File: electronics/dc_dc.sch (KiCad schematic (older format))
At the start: 14 parts

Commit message: Slightly change electronics
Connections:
- net labels added: VCC
- net labels removed: 5V
- wire segments 47 -> 41
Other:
- moved on the sheet: C?, D?, L?, R?
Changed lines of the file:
@@
 L Device:C C?
 U 1 1 5E8CFB92
-P 4500 3600
-F 0 "C?" H 4615 3646 50  0000 L CNN
-F 1 "C" H 4615 3555 50  0000 L CNN
-F 2 "" H 4538 3450 50  0001 C CNN
-F 3 "~" H 4500 3600 50  0001 C CNN
-	1    4500 3600
+P 4850 3000
+F 0 "C?" H 4965 3046 50  0000 L CNN
+F 1 "C" H 4965 2955 50  0000 L CNN
+F 2 "" H 4888 2850 50  0001 C CNN
+F 3 "~" H 4850 3000 50  0001 C CNN
+	1    4850 3000
 	1    0    0    -1
 $EndComp
@@
 L Device:C C?
 U 1 1 5E8D269D
-P 7250 3350
-F 0 "C?" H 7365 3396 50  0000 L CNN
-F 1 "C" H 7365 3305 50  0000 L CNN
-F 2 "" H 7288 3200 50  0001 C CNN
-F 3 "~" H 7250 3350 50  0001 C CNN
-	1    7250 3350
-	1    0    0    -1
+P 7250 3000
+F 0 "C?" H 7365 3046 50  0000 L CNN
+F 1 "C" H 7365 2955 50  0000 L CNN
+F 2 "" H 7288 2850 50  0001 C CNN
+F 3 "~" H 7250 3000 50  0001 C CNN
+	1    7250 3000
+	-1   0    0    1
 $EndComp
 $Comp
@@
 L Device:R R?
 U 1 1 5E8D49A8
-P 7600 3400
-F 0 "R?" H 7670 3446 50  0000 L CNN
-F 1 "R" H 7670 3355 50  0000 L CNN
-F 2 "" V 7530 3400 50  0001 C CNN
-F 3 "~" H 7600 3400 50  0001 C CNN
-	1    7600 3400
+P 7250 3550
+F 0 "R?" H 7320 3596 50  0000 L CNN
+F 1 "R" H 7320 3505 50  0000 L CNN
+F 2 "" V 7180 3550 50  0001 C CNN
+F 3 "~" H 7250 3550 50  0001 C CNN
+	1    7250 3550
 	1    0    0    -1
 $EndComp
@@
 	-1   0    0    1
 $EndComp
-Wire Wire Line
-	4500 3350 4300 3350
-Connection ~ 4500 3350
 $Comp
 L Device:R R?
@@
 	1    0    0    -1
 $EndComp
-$Comp
-L power:GND #PWR0102
-U 1 1 5E8DAC8B
-P 4500 3850
-F 0 "#PWR0102" H 4500 3600 50  0001 C CNN
-F 1 "GND" H 4505 3677 50  0000 C CNN
-F 2 "" H 4500 3850 50  0001 C CNN
-F 3 "" H 4500 3850 50  0001 C CNN
-	1    4500 3850
-	1    0    0    -1
-$EndComp
 Wire Wire Line
 	4850 4150 4850 3900
 Connection ~ 4850 3900
-Wire Wire Line
-	4850 3900 4700 3900
 Wire Wire Line
 	5700 3450 5700 3350
@@
 L Device:L L?
 U 1 1 5E8EE125
-P 6950 3100
-F 0 "L?" V 7140 3100 50  0000 C CNN
-F 1 "L" V 7049 3100 50  0000 C CNN
-F 2 "" H 6950 3100 50  0001 C CNN
-F 3 "~" H 6950 3100 50  0001 C CNN
-	1    6950 3100
+P 6750 3350
+F 0 "L?" V 6940 3350 50  0000 C CNN
+F 1 "L" V 6849 3350 50  0000 C CNN
+F 2 "" H 6750 3350 50  0001 C CNN
+F 3 "~" H 6750 3350 50  0001 C CNN
+	1    6750 3350
 	0    -1   -1   0
 $EndComp
@@
 L Device:D_Schottky D?
 U 1 1 5E8EE734
-P 6600 3350
-F 0 "D?" V 6554 3429 50  0000 L CNN
-F 1 "D_Schottky" V 6645 3429 50  0000 L CNN
-F 2 "" H 6600 3350 50  0001 C CNN
-F 3 "~" H 6600 3350 50  0001 C CNN
-	1    6600 3350
-	0    1    1    0
+P 6500 3000
+F 0 "D?" V 6454 3079 50  0000 L CNN
+F 1 "D_Schottky" V 6545 3079 50  0000 L CNN
+F 2 "" H 6500 3000 50  0001 C CNN
+F 3 "~" H 6500 3000 50  0001 C CNN
+	1    6500 3000
+	0    -1   -1   0
 $EndComp
 $Comp
 L power:GND #PWR0106
 U 1 1 5E8F0C8B
-P 6600 3550
-F 0 "#PWR0106" H 6600 3300 50  0001 C CNN
-F 1 "GND" H 6605 3377 50  0000 C CNN
-F 2 "" H 6600 3550 50  0001 C CNN
-F 3 "" H 6600 3550 50  0001 C CNN
-	1    6600 3550
-	1    0    0    -1
+P 6500 2750
+F 0 "#PWR0106" H 6500 2500 50  0001 C CNN
+F 1 "GND" H 6505 2577 50  0000 C CNN
+F 2 "" H 6500 2750 50  0001 C CNN
+F 3 "" H 6500 2750 50  0001 C CNN
+	1    6500 2750
+	-1   0    0    1
 $EndComp
 $Comp
 L power:GND #PWR0107
 U 1 1 5E8F68C8
-P 7250 3550
-F 0 "#PWR0107" H 7250 3300 50  0001 C CNN
-F 1 "GND" H 7255 3377 50  0000 C CNN
-F 2 "" H 7250 3550 50  0001 C CNN
-F 3 "" H 7250 3550 50  0001 C CNN
-	1    7250 3550
-	1    0    0    -1
-$EndComp
-Wire Wire Line
-	6600 3550 6600 3500
-Wire Wire Line
-	7250 3550 7250 3500
-Wire Wire Line
-	6300 3350 6300 3100
-Wire Wire Line
-	6300 3100 6600 3100
+P 7250 2750
+F 0 "#PWR0107" H 7250 2500 50  0001 C CNN
+F 1 "GND" H 7255 2577 50  0000 C CNN
+F 2 "" H 7250 2750 50  0001 C CNN
+F 3 "" H 7250 2750 50  0001 C CNN
+	1    7250 2750
+	-1   0    0    1
+$EndComp
+Wire Wire Line
+	6500 2750 6500 2850
+Wire Wire Line
+	7250 2750 7250 2850
 Connection ~ 6300 3350
 Wire Wire Line
-	6600 3200 6600 3100
-Connection ~ 6600 3100
-Wire Wire Line
-	6600 3100 6800 3100
-Wire Wire Line
-	7100 3100 7250 3100
-Wire Wire Line
-	7250 3100 7250 3200
-Wire Wire Line
 	6200 3800 7250 3800
 Wire Wire Line
 	7250 3800 7250 4000
 Wire Wire Line
-	7250 3800 7600 3800
-Wire Wire Line
-	7600 3800 7600 3550
-Connection ~ 7250 3800
-Wire Wire Line
-	7600 3250 7600 3100
-Wire Wire Line
-	7600 3100 7250 3100
-Connection ~ 7250 3100
+	7250 3800 7250 3700
 Wire Wire Line
 	7250 4300 7250 4700
@@
 $EndComp
 Wire Wire Line
-	4500 3350 4850 3350
-Wire Wire Line
 	4850 3350 4850 3450
 Connection ~ 4850 3350
 Wire Wire Line
-	4500 3350 4500 3450
-Wire Wire Line
 	4850 3750 4850 3900
-Wire Wire Line
-	7600 3100 7800 3100
-Connection ~ 7600 3100
-Wire Wire Line
-	4500 3850 4500 3750
-Text Label 7700 3100 0    50   ~ 0
-5V
-Text Label 4300 3350 0    50   ~ 0
+Text Label 8150 3350 0    50   ~ 0
+VCC
+Text Label 3250 3350 0    50   ~ 0
 BATT
-Wire Wire Line
-	4300 4300 4700 4300
-Wire Wire Line
-	4700 3900 4700 4300
-Text Label 4300 4300 0    50   ~ 0
+Text Label 3250 3900 0    50   ~ 0
 EN
 Wire Wire Line
@@
 Wire Wire Line
 	4850 4500 4850 4700
+Wire Wire Line
+	3250 3350 4850 3350
+Wire Wire Line
+	3250 3900 4850 3900
+Wire Wire Line
+	4850 3150 4850 3350
+Wire Wire Line
+	4850 2850 4850 2750
+$Comp
+L power:GND #PWR?
+U 1 1 5E932930
+P 4850 2750
+F 0 "#PWR?" H 4850 2500 50  0001 C CNN
+F 1 "GND" H 4855 2577 50  0000 C CNN
+F 2 "" H 4850 2750 50  0001 C CNN
+F 3 "" H 4850 2750 50  0001 C CNN
+	1    4850 2750
+	-1   0    0    1
+$EndComp
+Wire Wire Line
+	6300 3350 6500 3350
+Connection ~ 7250 3800
+Wire Wire Line
+	6900 3350 7250 3350
+Connection ~ 7250 3350
+Wire Wire Line
+	7250 3350 7250 3400
+Wire Wire Line
+	7250 3350 8250 3350
+Wire Wire Line
+	6500 3150 6500 3350
+Connection ~ 6500 3350
+Wire Wire Line
+	6500 3350 6600 3350
+Wire Wire Line
+	7250 3150 7250 3350
 $EndSCHEMATC

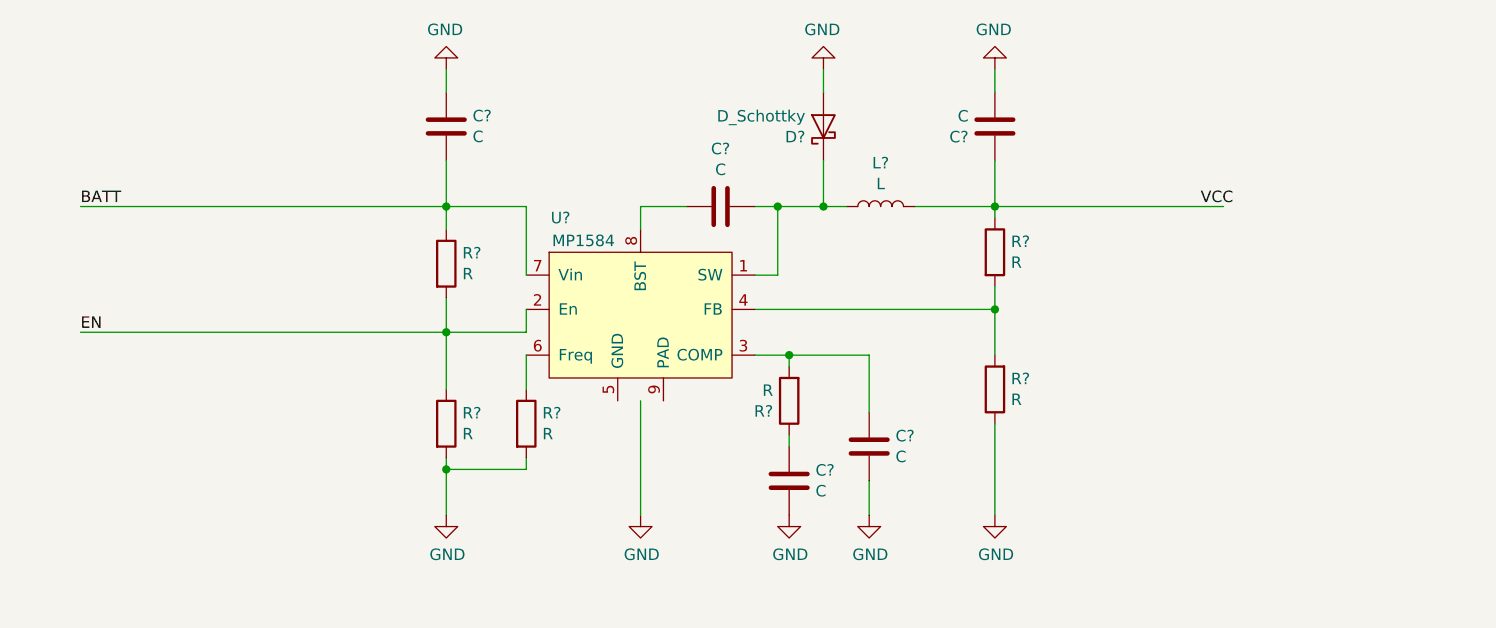
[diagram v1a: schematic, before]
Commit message: Update DCDC design, add a DCDC output calculator tool, add oled screen 3D models
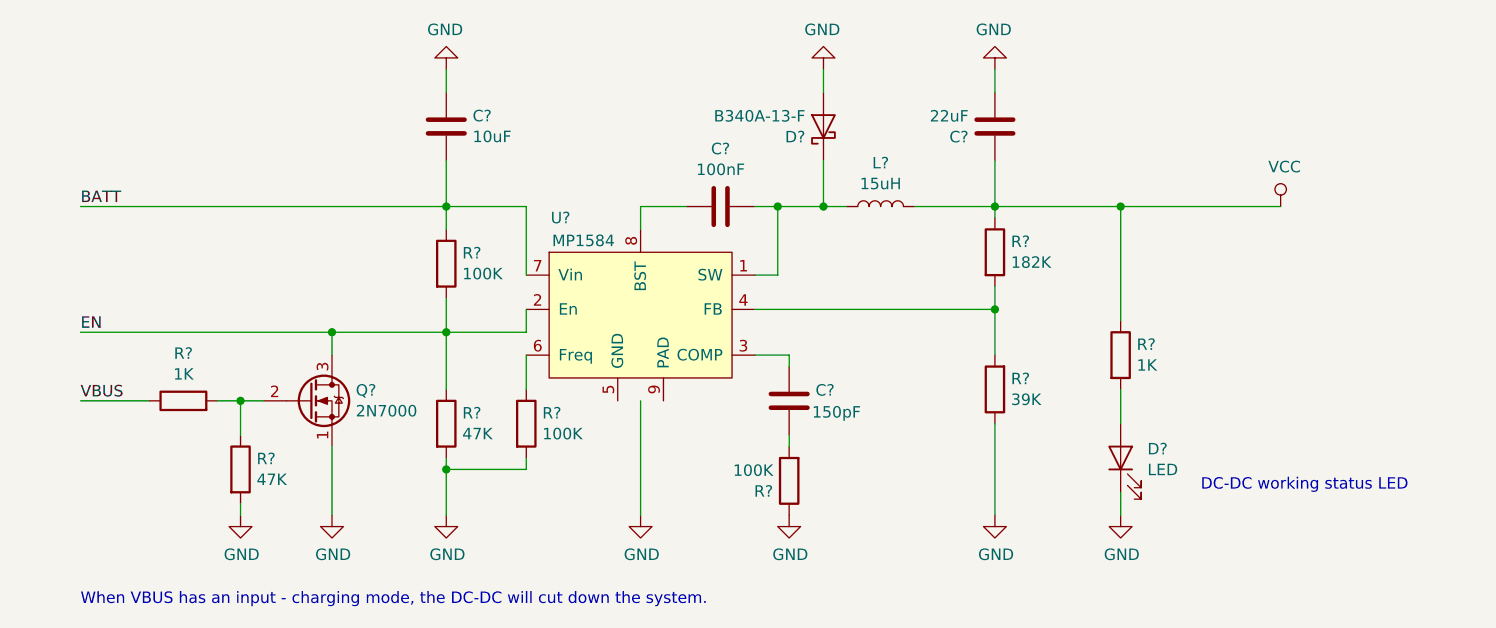
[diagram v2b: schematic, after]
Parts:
- removed C?: C, symbol Device:C
- added D?: LED, LED_SMD:LED_0805_2012Metric, symbol Device:LED
- added Q?: 2N7000, Package_TO_SOT_SMD:SOT-23, symbol Transistor_FET:2N7000
- added R? (x2): 1K, Resistor_SMD:R_0805_2012Metric, symbol Device:R
- added R?: 47K, Resistor_SMD:R_0805_2012Metric, symbol Device:R
- C?: value C -> 10uF; footprint (none) -> Capacitor_SMD:C_1206_3216Metric
- C?: value C -> 100nF; footprint (none) -> Capacitor_SMD:C_0805_2012Metric
- C?: value C -> 22uF; footprint (none) -> Capacitor_SMD:C_1206_3216Metric
- C?: value C -> 150pF; footprint (none) -> Capacitor_SMD:C_0805_2012Metric
- D?: value D_Schottky -> B340A-13-F; footprint (none) -> Diode_SMD:D_SMA
- L?: value L -> 15uH; footprint (none) -> Inductor_SMD:L_12x12mm_H6mm
- R? (x3): value R -> 100K; footprint (none) -> Resistor_SMD:R_0805_2012Metric
- R?: value R -> 47K; footprint (none) -> Resistor_SMD:R_0805_2012Metric
- R?: value R -> 182K; footprint (none) -> Resistor_SMD:R_0805_2012Metric
- R?: value R -> 39K; footprint (none) -> Resistor_SMD:R_0805_2012Metric
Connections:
- net labels added: VBUS
- wire segments 41 -> 50
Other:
- note added: "DC-DC working status LED"
- note added: "When VBUS has an input - charging mode, the DC-DC will cut down the system."
- moved on the sheet: C?, R?
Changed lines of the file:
@@
 P 4850 3000
 F 0 "C?" H 4965 3046 50  0000 L CNN
-F 1 "C" H 4965 2955 50  0000 L CNN
-F 2 "" H 4888 2850 50  0001 C CNN
+F 1 "10uF" H 4965 2955 50  0000 L CNN
+F 2 "Capacitor_SMD:C_1206_3216Metric" H 4888 2850 50  0001 C CNN
 F 3 "~" H 4850 3000 50  0001 C CNN
 	1    4850 3000
@@
 P 6050 3350
 F 0 "C?" V 5798 3350 50  0000 C CNN
-F 1 "C" V 5889 3350 50  0000 C CNN
-F 2 "" H 6088 3200 50  0001 C CNN
+F 1 "100nF" V 5889 3350 50  0000 C CNN
+F 2 "Capacitor_SMD:C_0805_2012Metric" H 6088 3200 50  0001 C CNN
 F 3 "~" H 6050 3350 50  0001 C CNN
 	1    6050 3350
@@
 P 4850 3600
 F 0 "R?" H 4920 3646 50  0000 L CNN
-F 1 "R" H 4920 3555 50  0000 L CNN
-F 2 "" V 4780 3600 50  0001 C CNN
+F 1 "100K" H 4920 3555 50  0000 L CNN
+F 2 "Resistor_SMD:R_0805_2012Metric" V 4780 3600 50  0001 C CNN
 F 3 "~" H 4850 3600 50  0001 C CNN
 	1    4850 3600
@@
 P 4850 4300
 F 0 "R?" H 4920 4346 50  0000 L CNN
-F 1 "R" H 4920 4255 50  0000 L CNN
-F 2 "" V 4780 4300 50  0001 C CNN
+F 1 "47K" H 4920 4255 50  0000 L CNN
+F 2 "Resistor_SMD:R_0805_2012Metric" V 4780 4300 50  0001 C CNN
 F 3 "~" H 4850 4300 50  0001 C CNN
 	1    4850 4300
@@
 P 7250 3000
 F 0 "C?" H 7365 3046 50  0000 L CNN
-F 1 "C" H 7365 2955 50  0000 L CNN
-F 2 "" H 7288 2850 50  0001 C CNN
+F 1 "22uF" H 7365 2955 50  0000 L CNN
+F 2 "Capacitor_SMD:C_1206_3216Metric" H 7288 2850 50  0001 C CNN
 F 3 "~" H 7250 3000 50  0001 C CNN
 	1    7250 3000
@@
 L Device:C C?
 U 1 1 5E8D2B29
-P 6350 4550
-F 0 "C?" H 6465 4596 50  0000 L CNN
-F 1 "C" H 6465 4505 50  0000 L CNN
-F 2 "" H 6388 4400 50  0001 C CNN
-F 3 "~" H 6350 4550 50  0001 C CNN
-	1    6350 4550
-	1    0    0    -1
-$EndComp
-$Comp
-L Device:C C?
-U 1 1 5E8D32A5
-P 6700 4400
-F 0 "C?" H 6815 4446 50  0000 L CNN
-F 1 "C" H 6815 4355 50  0000 L CNN
-F 2 "" H 6738 4250 50  0001 C CNN
-F 3 "~" H 6700 4400 50  0001 C CNN
-	1    6700 4400
+P 6350 4200
+F 0 "C?" H 6465 4246 50  0000 L CNN
+F 1 "150pF" H 6450 4150 50  0000 L CNN
+F 2 "Capacitor_SMD:C_0805_2012Metric" H 6388 4050 50  0001 C CNN
+F 3 "~" H 6350 4200 50  0001 C CNN
+	1    6350 4200
 	1    0    0    -1
 $EndComp
@@
 P 7250 3550
 F 0 "R?" H 7320 3596 50  0000 L CNN
-F 1 "R" H 7320 3505 50  0000 L CNN
-F 2 "" V 7180 3550 50  0001 C CNN
+F 1 "182K" H 7320 3505 50  0000 L CNN
+F 2 "Resistor_SMD:R_0805_2012Metric" V 7180 3550 50  0001 C CNN
 F 3 "~" H 7250 3550 50  0001 C CNN
 	1    7250 3550
@@
 L Device:R R?
 U 1 1 5E8D4DEA
-P 6350 4200
-F 0 "R?" H 6420 4246 50  0000 L CNN
-F 1 "R" H 6420 4155 50  0000 L CNN
-F 2 "" V 6280 4200 50  0001 C CNN
-F 3 "~" H 6350 4200 50  0001 C CNN
-	1    6350 4200
+P 6350 4550
+F 0 "R?" H 6420 4596 50  0000 L CNN
+F 1 "100K" H 6420 4505 50  0000 L CNN
+F 2 "Resistor_SMD:R_0805_2012Metric" V 6280 4550 50  0001 C CNN
+F 3 "~" H 6350 4550 50  0001 C CNN
+	1    6350 4550
 	-1   0    0    1
 $EndComp
@@
 P 5200 4300
 F 0 "R?" H 5270 4346 50  0000 L CNN
-F 1 "R" H 5270 4255 50  0000 L CNN
-F 2 "" V 5130 4300 50  0001 C CNN
+F 1 "100K" H 5270 4255 50  0000 L CNN
+F 2 "Resistor_SMD:R_0805_2012Metric" V 5130 4300 50  0001 C CNN
 F 3 "~" H 5200 4300 50  0001 C CNN
 	1    5200 4300
@@
 Wire Wire Line
 	5700 4200 5700 4700
-Wire Wire Line
-	6700 4000 6350 4000
-Connection ~ 6350 4000
-Wire Wire Line
-	6700 4000 6700 4250
-Wire Wire Line
-	6700 4550 6700 4700
-$Comp
-L power:GND #PWR0105
-U 1 1 5E8EBD06
-P 6700 4700
-F 0 "#PWR0105" H 6700 4450 50  0001 C CNN
-F 1 "GND" H 6705 4527 50  0000 C CNN
-F 2 "" H 6700 4700 50  0001 C CNN
-F 3 "" H 6700 4700 50  0001 C CNN
-	1    6700 4700
-	1    0    0    -1
-$EndComp
 $Comp
 L Device:R R?
@@
 P 7250 4150
 F 0 "R?" H 7180 4104 50  0000 R CNN
-F 1 "R" H 7180 4195 50  0000 R CNN
-F 2 "" V 7180 4150 50  0001 C CNN
+F 1 "39K" H 7180 4195 50  0000 R CNN
+F 2 "Resistor_SMD:R_0805_2012Metric" V 7180 4150 50  0001 C CNN
 F 3 "~" H 7250 4150 50  0001 C CNN
 	1    7250 4150
@@
 P 6750 3350
 F 0 "L?" V 6940 3350 50  0000 C CNN
-F 1 "L" V 6849 3350 50  0000 C CNN
-F 2 "" H 6750 3350 50  0001 C CNN
+F 1 "15uH" V 6849 3350 50  0000 C CNN
+F 2 "Inductor_SMD:L_12x12mm_H6mm" H 6750 3350 50  0001 C CNN
 F 3 "~" H 6750 3350 50  0001 C CNN
 	1    6750 3350
@@
 P 6500 3000
 F 0 "D?" V 6454 3079 50  0000 L CNN
-F 1 "D_Schottky" V 6545 3079 50  0000 L CNN
-F 2 "" H 6500 3000 50  0001 C CNN
+F 1 "B340A-13-F" V 6545 3079 50  0000 L CNN
+F 2 "Diode_SMD:D_SMA" H 6500 3000 50  0001 C CNN
 F 3 "~" H 6500 3000 50  0001 C CNN
 	1    6500 3000
@@
 Wire Wire Line
 	4850 3750 4850 3900
-Text Label 8150 3350 0    50   ~ 0
-VCC
 Text Label 3250 3350 0    50   ~ 0
 BATT
@@
 Wire Wire Line
 	3250 3350 4850 3350
-Wire Wire Line
-	3250 3900 4850 3900
 Wire Wire Line
 	4850 3150 4850 3350
@@
 	7250 3350 7250 3400
 Wire Wire Line
-	7250 3350 8250 3350
+	7250 3350 7800 3350
 Wire Wire Line
 	6500 3150 6500 3350
@@
 Wire Wire Line
 	7250 3150 7250 3350
+$Comp
+L power:VCC #PWR?
+U 1 1 5E935E86
+P 8500 3350
+F 0 "#PWR?" H 8500 3200 50  0001 C CNN
+F 1 "VCC" H 8517 3523 50  0000 C CNN
+F 2 "" H 8500 3350 50  0001 C CNN
+F 3 "" H 8500 3350 50  0001 C CNN
+	1    8500 3350
+	1    0    0    -1
+$EndComp
+$Comp
+L Device:R R?
+U 1 1 5E938B26
+P 7800 4000
+F 0 "R?" H 7870 4046 50  0000 L CNN
+F 1 "1K" H 7870 3955 50  0000 L CNN
+F 2 "Resistor_SMD:R_0805_2012Metric" V 7730 4000 50  0001 C CNN
+F 3 "~" H 7800 4000 50  0001 C CNN
+	1    7800 4000
+	1    0    0    -1
+$EndComp
+$Comp
+L Device:LED D?
+U 1 1 5E939213
+P 7800 4450
+F 0 "D?" V 7839 4333 50  0000 R CNN
+F 1 "LED" V 7748 4333 50  0000 R CNN
+F 2 "LED_SMD:LED_0805_2012Metric" H 7800 4450 50  0001 C CNN
+F 3 "~" H 7800 4450 50  0001 C CNN
+	1    7800 4450
+	0    -1   -1   0
+$EndComp
+Wire Wire Line
+	7800 4150 7800 4300
+Wire Wire Line
+	7800 4600 7800 4700
+$Comp
+L power:GND #PWR?
+U 1 1 5E93DD7B
+P 7800 4700
+F 0 "#PWR?" H 7800 4450 50  0001 C CNN
+F 1 "GND" H 7805 4527 50  0000 C CNN
+F 2 "" H 7800 4700 50  0001 C CNN
+F 3 "" H 7800 4700 50  0001 C CNN
+	1    7800 4700
+	1    0    0    -1
+$EndComp
+Wire Wire Line
+	7800 3850 7800 3350
+Connection ~ 7800 3350
+Wire Wire Line
+	7800 3350 8500 3350
+$Comp
+L Transistor_FET:2N7000 Q?
+U 1 1 5E941285
+P 4250 4200
+F 0 "Q?" H 4454 4246 50  0000 L CNN
+F 1 "2N7000" H 4454 4155 50  0000 L CNN
+F 2 "Package_TO_SOT_SMD:SOT-23" H 4450 4125 50  0001 L CIN
+F 3 "https://www.fairchildsemi.com/datasheets/2N/2N7000.pdf" H 4250 4200 50  0001 L CNN
+	1    4250 4200
+	1    0    0    -1
+$EndComp
+$Comp
+L power:GND #PWR?
+U 1 1 5E94311E
+P 4350 4700
+F 0 "#PWR?" H 4350 4450 50  0001 C CNN
+F 1 "GND" H 4355 4527 50  0000 C CNN
+F 2 "" H 4350 4700 50  0001 C CNN
+F 3 "" H 4350 4700 50  0001 C CNN
+	1    4350 4700
+	1    0    0    -1
+$EndComp
+Wire Wire Line
+	4350 4400 4350 4700
+Wire Wire Line
+	4350 3900 4350 4000
+$Comp
+L Device:R R?
+U 1 1 5E9453A6
+P 3700 4200
+F 0 "R?" V 3907 4200 50  0000 C CNN
+F 1 "1K" V 3816 4200 50  0000 C CNN
+F 2 "Resistor_SMD:R_0805_2012Metric" V 3630 4200 50  0001 C CNN
+F 3 "~" H 3700 4200 50  0001 C CNN
+	1    3700 4200
+	0    -1   -1   0
+$EndComp
+$Comp
+L Device:R R?
+U 1 1 5E94608A
+P 3950 4500
+F 0 "R?" H 4020 4546 50  0000 L CNN
+F 1 "47K" H 4020 4455 50  0000 L CNN
+F 2 "Resistor_SMD:R_0805_2012Metric" V 3880 4500 50  0001 C CNN
+F 3 "~" H 3950 4500 50  0001 C CNN
+	1    3950 4500
+	1    0    0    -1
+$EndComp
+Connection ~ 4350 3900
+Wire Wire Line
+	4350 3900 4850 3900
+Wire Wire Line
+	3250 3900 4350 3900
+$Comp
+L power:GND #PWR?
+U 1 1 5E94BF0D
+P 3950 4700
+F 0 "#PWR?" H 3950 4450 50  0001 C CNN
+F 1 "GND" H 3955 4527 50  0000 C CNN
+F 2 "" H 3950 4700 50  0001 C CNN
+F 3 "" H 3950 4700 50  0001 C CNN
+	1    3950 4700
+	1    0    0    -1
+$EndComp
+Wire Wire Line
+	3850 4200 3950 4200
+Wire Wire Line
+	3950 4350 3950 4200
+Connection ~ 3950 4200
+Wire Wire Line
+	3950 4200 4050 4200
+Wire Wire Line
+	3950 4650 3950 4700
+Wire Wire Line
+	3550 4200 3250 4200
+Text Label 3250 4200 0    50   ~ 0
+VBUS
+Text Notes 3250 5100 0    50   ~ 0
+When VBUS has an input - charging mode, the DC-DC will cut down the system.
+Text Notes 8150 4600 0    50   ~ 0
+DC-DC working status LED
 $EndSCHEMATC

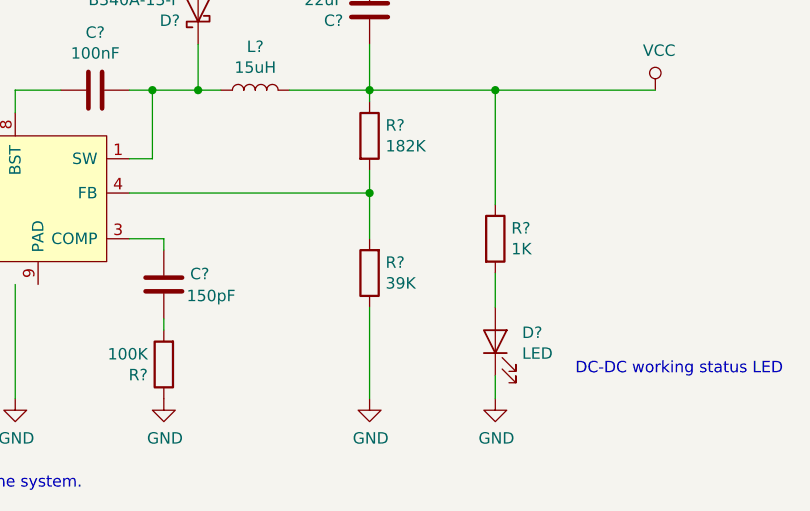
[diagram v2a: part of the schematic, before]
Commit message: Change to electronics, and adding pi dimensions into documents
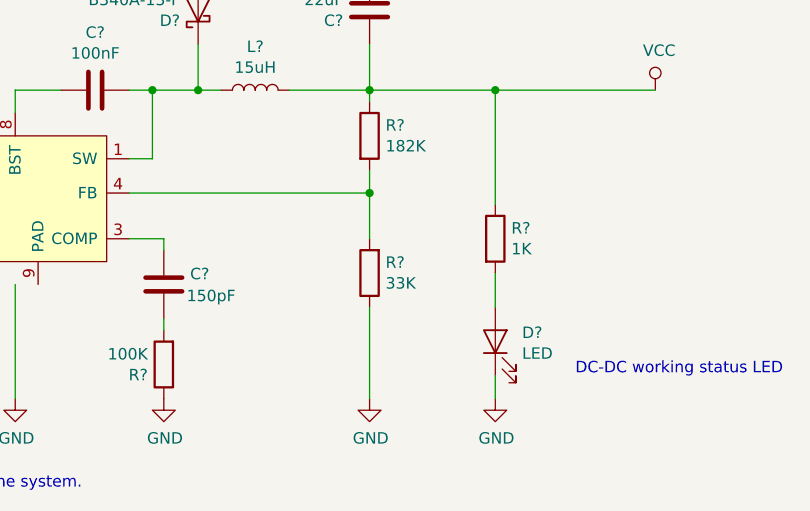
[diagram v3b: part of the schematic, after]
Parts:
- R?: value 39K -> 33K
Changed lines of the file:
@@
 $Descr A4 11693 8268
 encoding utf-8
-Sheet 2 5
+Sheet 2 4
 Title ""
 Date ""
@@
 $EndComp
 $Comp
-L power:GND #PWR0101
+L power:GND #PWR?
 U 1 1 5E8D8C44
 P 4850 4700
-F 0 "#PWR0101" H 4850 4450 50  0001 C CNN
+F 0 "#PWR?" H 4850 4450 50  0001 C CNN
 F 1 "GND" H 4855 4527 50  0000 C CNN
 F 2 "" H 4850 4700 50  0001 C CNN
@@
 	6300 3350 6200 3350
 $Comp
-L power:GND #PWR0103
+L power:GND #PWR?
 U 1 1 5E8E265E
 P 5700 4700
-F 0 "#PWR0103" H 5700 4450 50  0001 C CNN
+F 0 "#PWR?" H 5700 4450 50  0001 C CNN
 F 1 "GND" H 5705 4527 50  0000 C CNN
 F 2 "" H 5700 4700 50  0001 C CNN
@@
 	6350 4350 6350 4400
 $Comp
-L power:GND #PWR0104
+L power:GND #PWR?
 U 1 1 5E8E80EC
 P 6350 4700
-F 0 "#PWR0104" H 6350 4450 50  0001 C CNN
+F 0 "#PWR?" H 6350 4450 50  0001 C CNN
 F 1 "GND" H 6355 4527 50  0000 C CNN
 F 2 "" H 6350 4700 50  0001 C CNN
@@
 P 7250 4150
 F 0 "R?" H 7180 4104 50  0000 R CNN
-F 1 "39K" H 7180 4195 50  0000 R CNN
+F 1 "33K" H 7180 4195 50  0000 R CNN
 F 2 "Resistor_SMD:R_0805_2012Metric" V 7180 4150 50  0001 C CNN
 F 3 "~" H 7250 4150 50  0001 C CNN
@@
 $EndComp
 $Comp
-L power:GND #PWR0106
+L power:GND #PWR?
 U 1 1 5E8F0C8B
 P 6500 2750
-F 0 "#PWR0106" H 6500 2500 50  0001 C CNN
+F 0 "#PWR?" H 6500 2500 50  0001 C CNN
 F 1 "GND" H 6505 2577 50  0000 C CNN
 F 2 "" H 6500 2750 50  0001 C CNN
@@
 $EndComp
 $Comp
-L power:GND #PWR0107
+L power:GND #PWR?
 U 1 1 5E8F68C8
 P 7250 2750
-F 0 "#PWR0107" H 7250 2500 50  0001 C CNN
+F 0 "#PWR?" H 7250 2500 50  0001 C CNN
 F 1 "GND" H 7255 2577 50  0000 C CNN
 F 2 "" H 7250 2750 50  0001 C CNN
@@
 	7250 4300 7250 4700
 $Comp
-L power:GND #PWR0108
+L power:GND #PWR?
 U 1 1 5E8FFCF0
 P 7250 4700
-F 0 "#PWR0108" H 7250 4450 50  0001 C CNN
+F 0 "#PWR?" H 7250 4450 50  0001 C CNN
 F 1 "GND" H 7255 4527 50  0000 C CNN
 F 2 "" H 7250 4700 50  0001 C CNN
